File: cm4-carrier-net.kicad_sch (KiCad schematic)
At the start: 69 parts, among them J1 USB_C_Receptacle_USB2.0, J2 Conn_01x15_MountingPin, J2 Micro_SD_Card, J3 Abracon_ARJM11-502, J4 20021121-00010C4LF, J5 block, J6 USB_A, Q1 DMP2066LSN, Q2 FDMT800152DC, Q3 FDMT800152DC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

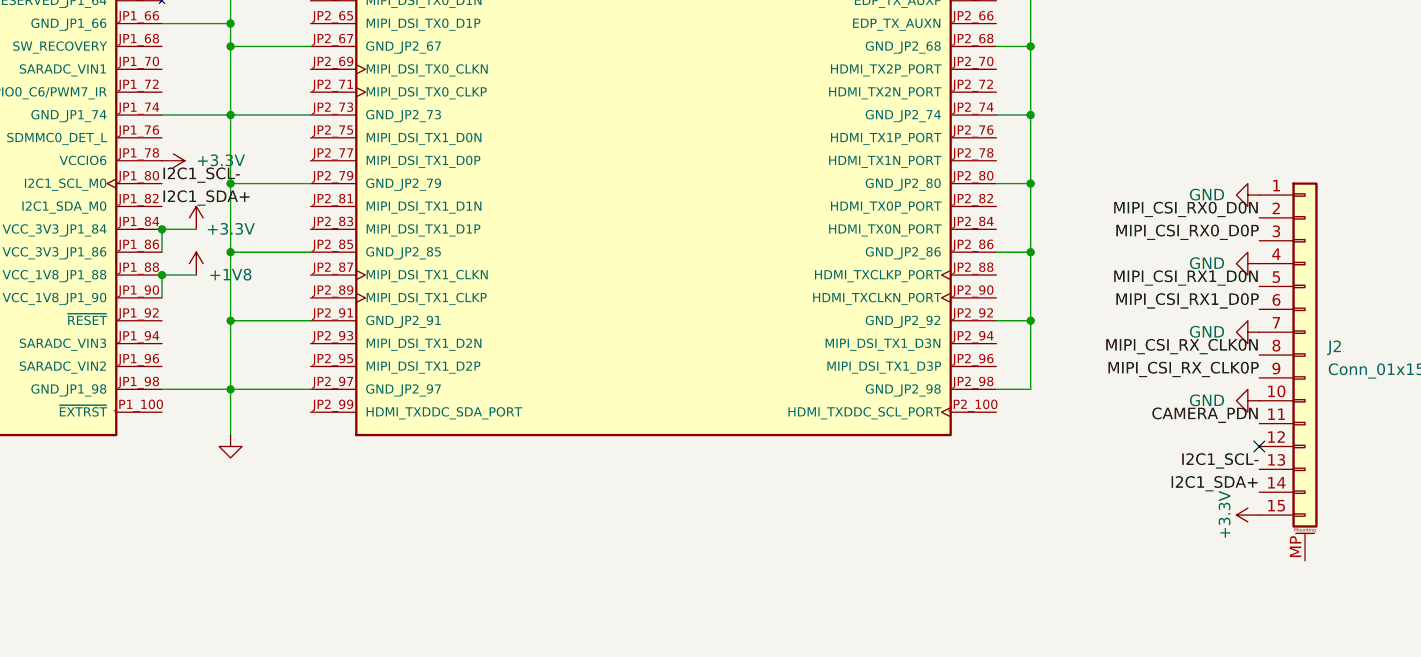
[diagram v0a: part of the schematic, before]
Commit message: tuned length of traces and pairs
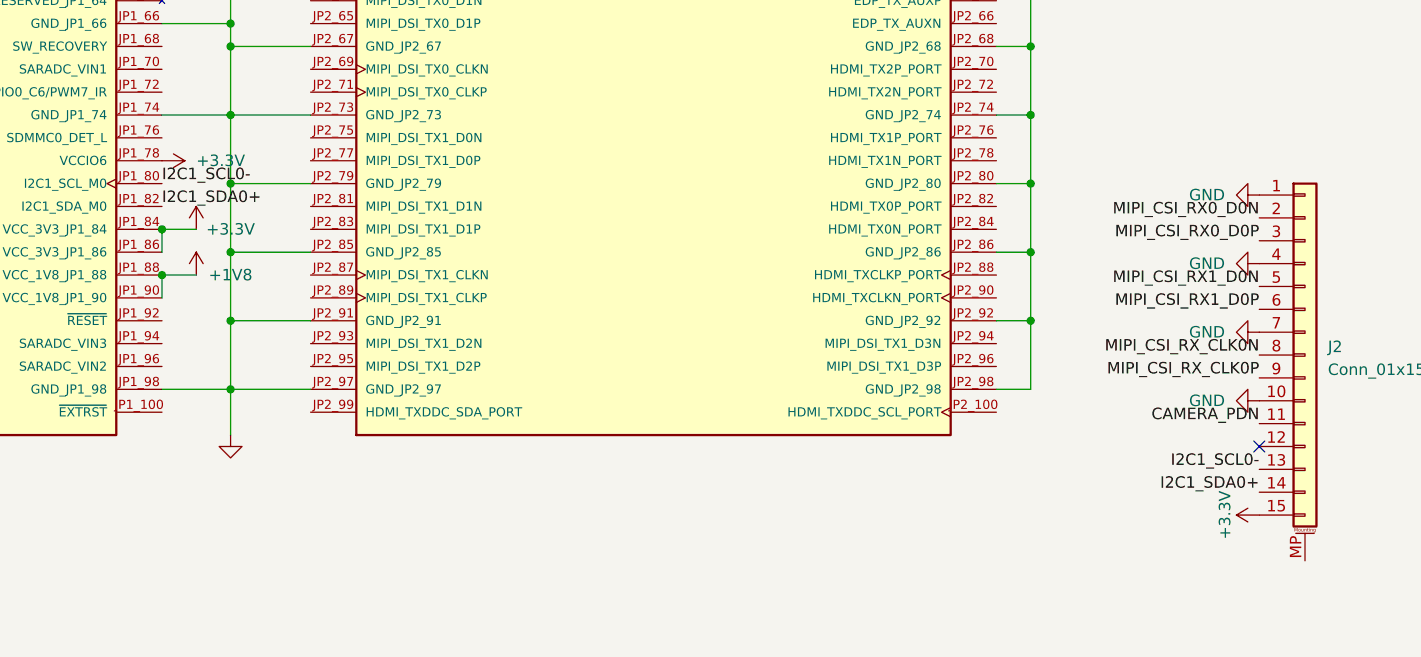
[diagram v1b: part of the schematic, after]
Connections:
- net I2C1_SCL- renamed I2C1_SCL0-
- net I2C1_SDA+ renamed I2C1_SDA0+
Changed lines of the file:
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@@
     (effects (font (size 1.27 1.27)) (justify right bottom))
   )
-  (label "I2C1_SDA+" (at 508 161.29 180) (fields_autoplaced)
+  (label "I2C1_SDA0+" (at 508 161.29 180) (fields_autoplaced)
     (effects (font (size 1.27 1.27)) (justify right bottom))
   )
@@
     (effects (font (size 1.27 1.27)) (justify right bottom))
   )
-  (label "I2C1_SCL-" (at 386.08 127 0) (fields_autoplaced)
+  (label "I2C1_SCL0-" (at 386.08 127 0) (fields_autoplaced)
     (effects (font (size 1.27 1.27)) (justify left bottom))
   )
@@
     (effects (font (size 1.27 1.27)) (justify right bottom))
   )
-  (label "I2C1_SDA+" (at 386.08 129.54 0) (fields_autoplaced)
+  (label "I2C1_SDA0+" (at 386.08 129.54 0) (fields_autoplaced)
     (effects (font (size 1.27 1.27)) (justify left bottom))
   )
@@
     (effects (font (size 1.27 1.27)) (justify right bottom))
   )
-  (label "I2C1_SCL-" (at 508 158.75 180) (fields_autoplaced)
+  (label "I2C1_SCL0-" (at 508 158.75 180) (fields_autoplaced)
     (effects (font (size 1.27 1.27)) (justify right bottom))
   )

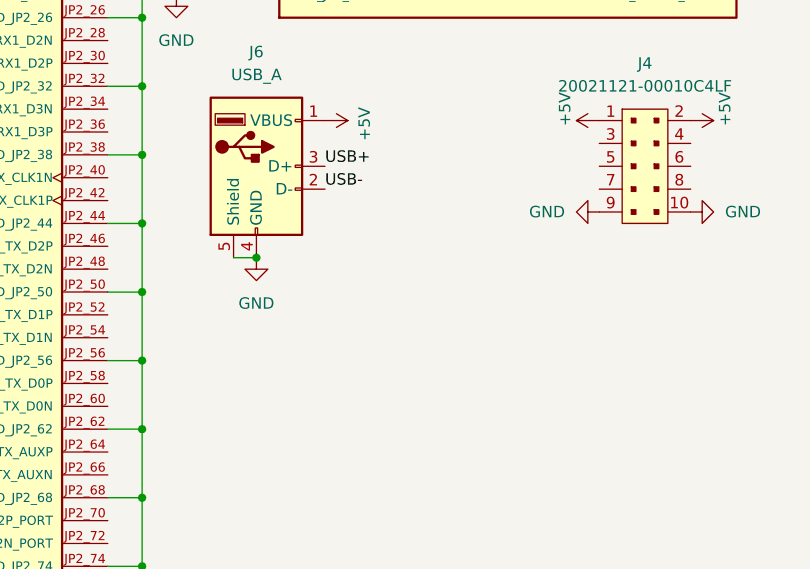
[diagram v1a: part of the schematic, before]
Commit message: added tvs on the usb a
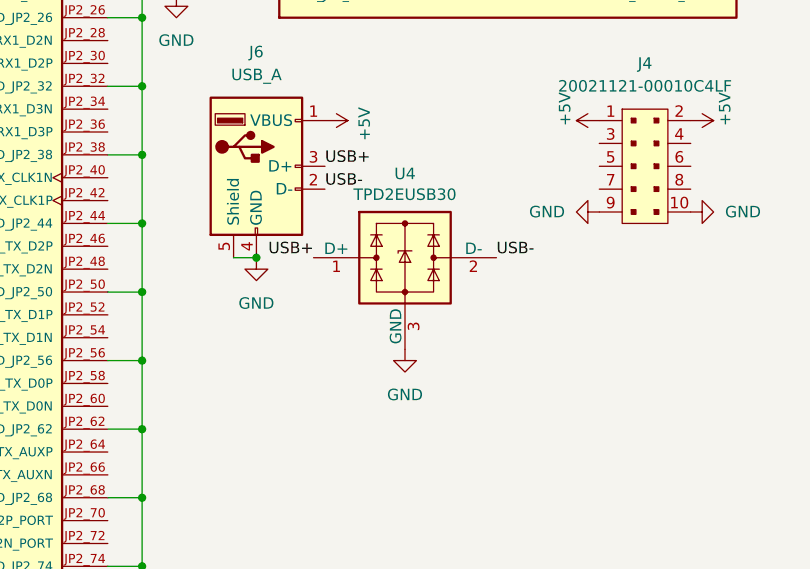
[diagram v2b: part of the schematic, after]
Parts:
- added U4: TPD2EUSB30, Package_TO_SOT_SMD:Texas_DRT-3, symbol Power_Protection:TPD2EUSB30
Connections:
- net GND: now also U4.3 (GND)
- net USB+: now also U4.1 (D+)
- net USB-: now also U4.2 (D-)
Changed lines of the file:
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@@
     (effects (font (size 1.27 1.27)) (justify left bottom))
   )
+  (label "USB-" (at 521.97 85.09 0) (fields_autoplaced)
+    (effects (font (size 1.27 1.27)) (justify left bottom))
+  )
   (label "MIPI_CSI_RX_CLK0P" (at 508 148.59 180) (fields_autoplaced)
     (effects (font (size 1.27 1.27)) (justify right bottom))
@@
     (effects (font (size 1.27 1.27)) (justify left bottom))
   )
+  (label "USB+" (at 501.65 85.09 180) (fields_autoplaced)
+    (effects (font (size 1.27 1.27)) (justify right bottom))
+  )
   (label "SD_D3" (at 95.25 73.66 180) (fields_autoplaced)
     (effects (font (size 1.27 1.27)) (justify right bottom))
@@
     )
   )
+  (symbol (lib_id "power:GND") (at 511.81 95.25 0) (unit 1)
+    (in_bom yes) (on_board yes) (dnp no) (fields_autoplaced)
+    (property "Reference" "#PWR031" (at 511.81 101.6 0)
+      (effects (font (size 1.27 1.27)) hide)
+    )
+    (property "Value" "GND" (at 511.81 100.33 0)
+      (effects (font (size 1.27 1.27)))
+    )
+    (property "Footprint" "" (at 511.81 95.25 0)
+      (effects (font (size 1.27 1.27)) hide)
+    )
+    (property "Datasheet" "" (at 511.81 95.25 0)
+      (effects (font (size 1.27 1.27)) hide)
+    )
+    (pin "1")
+    (instances
+      (project "cm4-carrier-net"
+        (path "/a58a5c23-cf42-4abb-bf4c-19a657300252"
+          (reference "#PWR031") (unit 1)
+        )
+      )
+    )
+  )
   (symbol (lib_id "power:GND") (at 179.07 167.64 90) (unit 1)
     (in_bom yes) (on_board yes) (dnp no)
@@
         )
       )
+    )
+  )
+  (symbol (lib_id "Power_Protection:TPD2EUSB30") (at 511.81 85.09 0) (unit 1)
+    (in_bom yes) (on_board yes) (dnp no)
+    (property "Reference" "U4" (at 511.81 75.7682 0)
+      (effects (font (size 1.27 1.27)))
+    )
+    (property "Value" "TPD2EUSB30" (at 511.81 78.0796 0)
+      (effects (font (size 1.27 1.27)))
+    )
+    (property "Footprint" "Package_TO_SOT_SMD:Texas_DRT-3" (at 492.76 92.71 0)
+      (effects (font (size 1.27 1.27)) hide)
+    )
+    (property "Datasheet" "http://www.ti.com/lit/ds/symlink/tpd2eusb30a.pdf" (at 511.81 85.09 0)
+      (effects (font (size 1.27 1.27)) hide)
+    )
+    (pin "1")
+    (pin "2")
+    (pin "3")
+    (instances
+      (project "cm4-carrier-net"
+        (path "/a58a5c23-cf42-4abb-bf4c-19a657300252"
+          (reference "U4") (unit 1)
+        )
+      )

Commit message: added some fun thingies
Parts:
- removed J4: 20021121-00010C4LF, digikey-footprints:PinHeader_2x5_P1.27mm, symbol dk_Rectangular-Connectors-Headers-Male-Pins:20021121-00010C4LF
- added C12, C13: 22u, Capacitor_SMD:C_0805_2012Metric, symbol Device:C_Small
- added M1: Fan, Connector_PinHeader_2.54mm:PinHeader_1x02_P2.54mm_Vertical, symbol Motor:Fan
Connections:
- net +3.3V: now also C12.1
- net +5V: now also C13.1, M1.1 (+)
- net GND: now also J2.MP (MountPin), C12.2, C13.2, M1.2 (-)

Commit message: redesigned pcb
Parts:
- removed C3: 100n, Capacitor_SMD:C_0805_2012Metric, symbol Device:C_Small
- removed C4: 22u, Capacitor_SMD:C_0805_2012Metric, symbol Device:C_Small
- removed D4: SD ON, LED_SMD:LED_0603_1608Metric, symbol Device:LED_Small
- removed FID1, FID2, FID3, FID4, FID5, FID6: Fiducial, Fiducial:Fiducial_0.75mm_Mask1.5mm, symbol Mechanical:Fiducial
- removed J2: Micro_SD_Card, Connector_Card:microSD_HC_Molex_104031-0811, symbol Connector:Micro_SD_Card
- removed J3: Abracon_ARJM11-502, jkiv-library:RJ45_Abracon_ARJM11, symbol cm4-carrier-net-rescue:Abracon_ARJM11-502-jkiv-abracon
- removed JP5: SolderJumper_2_Bridged, Jumper:SolderJumper-2_P1.3mm_Bridged2Bar_RoundedPad1.0x1.5mm, symbol Jumper:SolderJumper_2_Bridged
- removed LOGO1: Logo_Open_Hardware_Small, Symbol:OSHW-Symbol_6.7x6mm_Copper, symbol Graphic:Logo_Open_Hardware_Small
- removed Q1: DMP2066LSN, Package_TO_SOT_SMD:SC-59, symbol Device:Q_PMOS_GSD
- removed Q2, Q3: FDMT800152DC, Package_TO_SOT_SMD:PQFN_8x8, symbol Transistor_FET:FDMT800152DC
- removed R12, R8: 220R, Resistor_SMD:R_0603_1608Metric, symbol Device:R_Small_US
- removed R18: 2740kOhm, Resistor_SMD:R_0603_1608Metric, symbol Device:R_Small_US
- removed R19: 215kOhm, Resistor_SMD:R_0603_1608Metric, symbol Device:R_Small_US
- removed R20: 84.5kOhm, Resistor_SMD:R_0603_1608Metric, symbol Device:R_Small_US
- removed U2: LTC4365TS8, Package_TO_SOT_SMD:TSOT-23-8, symbol Power_Management:LTC4365TS8
- added C4: 22uF, Capacitor_SMD:C_1206_3216Metric, symbol Device:C
- added D5, D6: LED, Diode_SMD:D_1206_3216Metric_Pad1.42x1.75mm_HandSolder, symbol Device:LED
- added J3: 54602-908LF, digikey-footprints:Ethernet_Jack_54602-908LF, symbol dk_Modular-Connectors-Jacks:54602-908LF
- added Q2: LTC4412ES6_TRMPBF, digikey-footprints:SOT-23-6, symbol dk_PMIC-OR-Controllers-Ideal-Diodes:LTC4412ES6_TRMPBF
- added Q3, Q4: IRLML6401TRPBF, digikey-footprints:SOT-23-3, symbol dk_Transistors-FETs-MOSFETs-Single:IRLML6401TRPBF
- J1: footprint jkiv-library:USB_C_Receptacle_GCT-USB4105 -> Connector_USB:USB_C_Receptacle_G-Switch_GT-USB-7010ASV
- J6: footprint Connector_USB:USB_A_Receptacle_GCT_USB1046 -> Connector_USB:USB_A_Wuerth_614004134726_Horizontal
- R17: value 510kOhm -> 470kOhm
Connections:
- net +12V: now also J5.2 (Pin_2)
- net +3.3V: now also D5.2 (A), D6.2 (A)
- net +5V: now also R17.1, C4.1, Q2.6 (SENSE), Q3.2 (S), Q4.2 (S); no longer C1.1, C10.2, C2.1, FB1.1, JP6.1 (A)
- net E0_TR0+: now also J3.1
- net E0_TR0-: now also J3.2
- net E0_TR1+: now also J3.3
- net E0_TR1-: now also J3.4
- net E0_TR2+: now also J3.5
- net E0_TR2-: now also J3.6
- net E0_TR3+: now also J3.7
- net E0_TR3-: now also J3.8
- net GND: now also C4.2, Q2.2 (GND), Q2.3 (CTL)
- net at R4.1: now also D5.1 (K)
- net at R3.1: now also D6.1 (K)
- net at R17.2: now also Q2.4 (STAT), Q4.1 (G)
- net HDMI_SCL: now reaches U3.JP2_100 (HDMI_TXDDC_SCL_PORT)
- net HDMI_CEC: now reaches U3.JP2_51 (HDMI_CEC_PORT)
- net HDMI_D2+: now reaches U3.JP2_70 (HDMI_TX2P_PORT)
- net HDMI_D2-: now reaches U3.JP2_72 (HDMI_TX2N_PORT)
- net HDMI_D1+: now reaches U3.JP2_76 (HDMI_TX1P_PORT)
- net HDMI_D1-: now reaches U3.JP2_78 (HDMI_TX1N_PORT)
- net HDMI_D0+: now reaches U3.JP2_82 (HDMI_TX0P_PORT)
- net HDMI_D0-: now reaches U3.JP2_84 (HDMI_TX0N_PORT)
- net HDMI_CK+: now reaches U3.JP2_88 (HDMI_TXCLKP_PORT)
- net HDMI_CK-: now reaches U3.JP2_90 (HDMI_TXCLKN_PORT)
- net HDMI_SDA: now reaches U3.JP2_99 (HDMI_TXDDC_SDA_PORT)
- new net: Q2.5 (GATE), Q3.1 (G)
- new net 5v_From_Bot: C10.2, JP6.1 (A), Q2.1 (VIN), Q3.3 (D)
- new net 5v_From_USB: C1.1, C2.1, FB1.1, Q4.3 (D)
- no-connect marks 4 -> 3
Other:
- note added: "Camera"
- note added: "Power Delivery"
- note removed: "Extensions"
- note removed: "Just pretend that everything outside of the outline is in here ;)"
- note removed: "MicroSD Storage"
- moved on the sheet: C10, C11, C12, C13, C6, C7, C8, C9, H1, H2, H3, H4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
